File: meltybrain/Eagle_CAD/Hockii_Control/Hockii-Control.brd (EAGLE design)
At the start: 74 x 37 mm, 66 parts, among them J1 SM03B-SRSS-TB(LF)(SN), J2 SM04B-SRSS-TB(LF)(SN), J4 SM04B-SRSS-TB(LF)(SN), J7 SM02B-SRSS-TB(LF)(SN), J8 SM02B-SRSS-TB(LF)(SN), U13 TMP235A4DCKR, U14 ADXL375, U15 NL27WZ32USG, U16 ADXL375, U17 ADXL375, U18 NL27WZ32USG, U19 ADXL375, U2 TEENSY_4.1, U3 AP2210K-5.0TRG1, U5 TXS0104ED, U6 LDL212PU50R, U7 LIS3MDLTR, U8 BA50DD0WHFP-TR, X1 22-23-2021

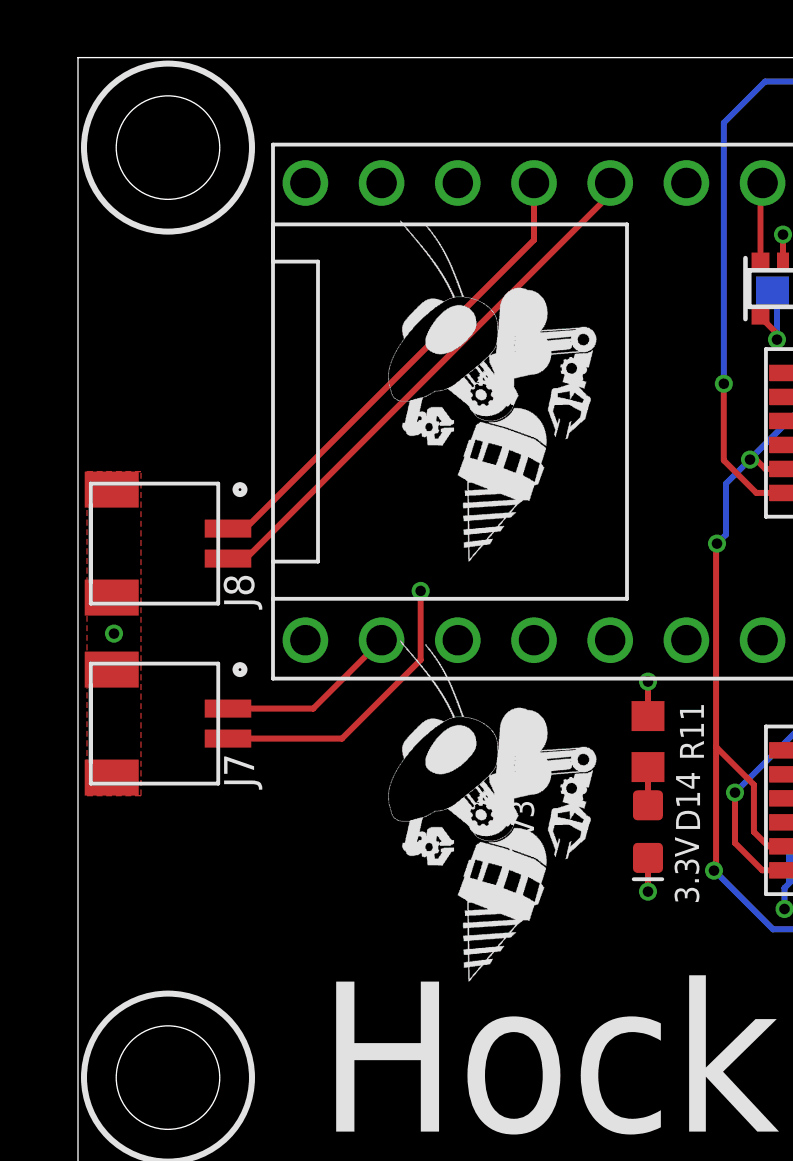
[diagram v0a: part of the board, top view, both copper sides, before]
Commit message: add VESC JST
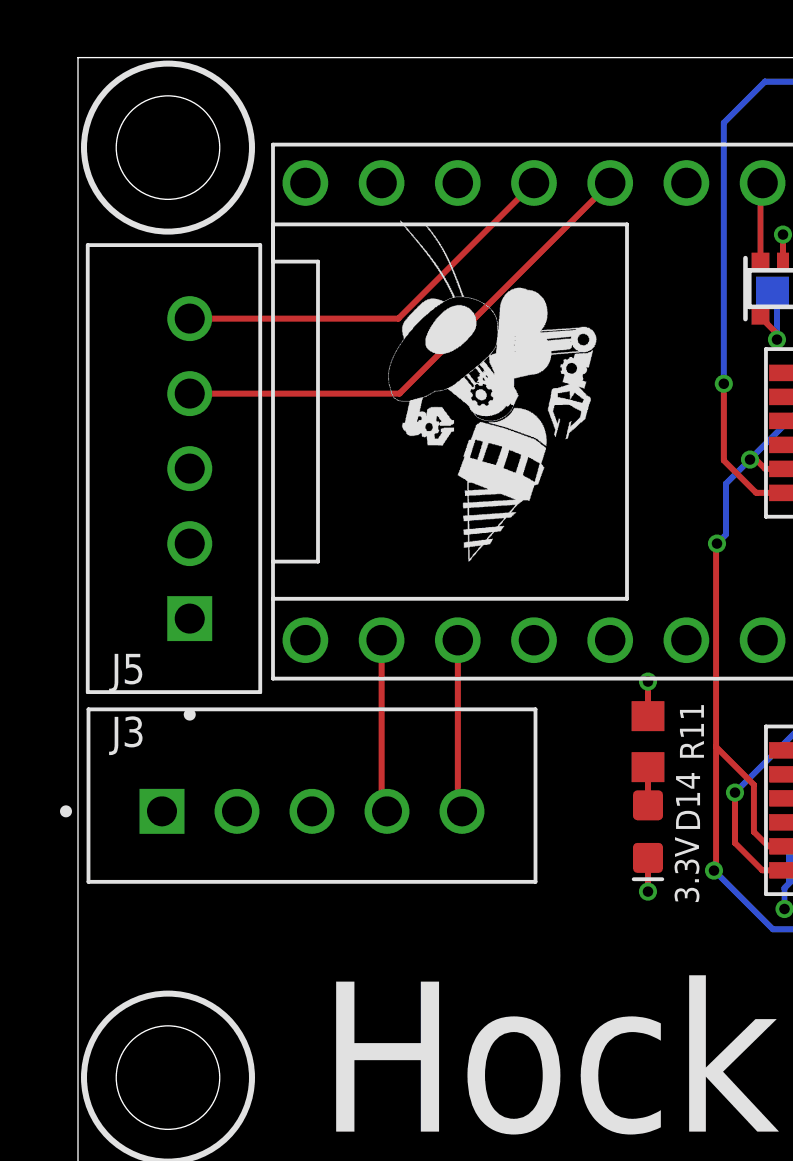
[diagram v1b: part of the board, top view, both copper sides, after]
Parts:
- removed J7, J8: SM02B-SRSS-TB(LF)(SN), Hocki_Library:SM02B-SRSS-TB(LF)(SN)
- removed U$1: (no value), RoboJackets-Aesthetics:ROBOBUZZ_0.6X
- added J3, J5: B5B-XH-A(LF)(SN), Hocki_Library:JST_B5B-XH-A(LF)(SN)
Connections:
- removed net ESC_L: J8.1, U2.29
- removed net ESC_R: J7.2, U2.24
- removed net ESC_TEL_L: J8.2, U2.28
- removed net ESC_TEL_R: J7.1, U2.34
- new net VESC1_RX: J5.4, U2.28
- new net VESC1_TX: J5.5, U2.29
- new net VESC_RX: J3.4, U2.34
- new net VESC_TX: J3.5, U2.35
- net 3.3V: now also J3.2, J5.2
- net 5V: now also J3.1, J5.1
- net GND: now also J3.3, J5.3; no longer J7.S1, J7.S2, J8.S1, J8.S2
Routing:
- net 5V: track 23.3 -> 59.2 mm
- net ESC_R: track 32.4 -> 0.00 mm, vias 1 -> 0
- net ESC_TEL_L: track 18.1 -> 0.00 mm
- net VESC1_RX: track 0.00 -> 16.9 mm
- net ESC_L: track 16.1 -> 0.00 mm
- net VESC1_TX: track 0.00 -> 13.3 mm
- net ESC_TEL_R: track 6.06 -> 0.00 mm
- net VESC_RX: track 0.00 -> 5.78 mm
- net VESC_TX: track 0.00 -> 5.76 mm
- net GND: vias 52 -> 51
- removed copper zone on layer 15, net +3V3
- removed copper zone on layer 1, net GND
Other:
- board text added: "Hockii Control V1.1"
- board text removed: "3V3"
- board text removed: "Hockii Control V1"
